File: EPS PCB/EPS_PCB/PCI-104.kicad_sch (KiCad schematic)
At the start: 10 parts, among them J1 Conn_02x32_Row_Letter_First, J2 Conn_02x20_Row_Letter_First

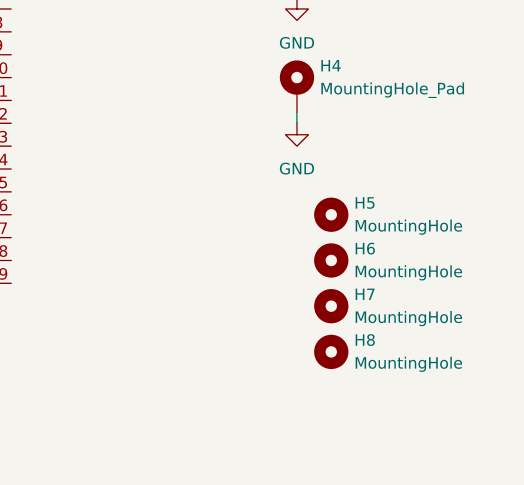
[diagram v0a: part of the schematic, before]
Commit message: PDR Update
Added Current Measurement, Hysteresis, EFuses
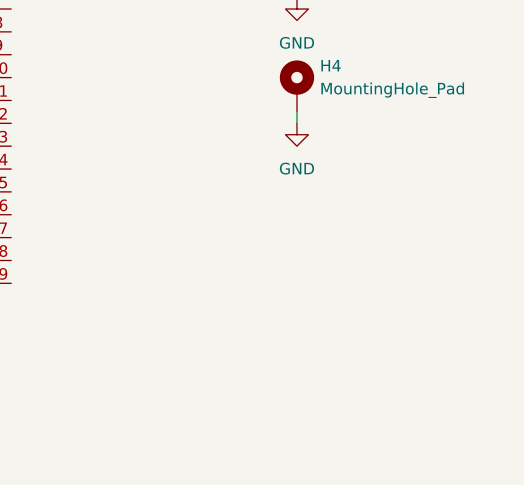
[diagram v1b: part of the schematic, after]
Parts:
- removed H5, H6, H7, H8: MountingHole, MountingHole:MountingHole_2mm, symbol Mechanical:MountingHole
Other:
- company: GU Orbit -> UW Huskysat
